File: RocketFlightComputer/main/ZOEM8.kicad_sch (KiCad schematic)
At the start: 11 parts

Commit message: Well I added a bunch of sensors, some connectors for battery, pyro channels mosfets, etc
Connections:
- net ZOEM8_SCL renamed ZOEM8_SCL1
- net ZOEM8_SDA renamed ZOEM8_SDA1
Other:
- note added: "Max Current: 67 mA"
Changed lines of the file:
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@@
     (effects (font (size 2.032 2.032)) (justify left bottom))
+  )
+  (text "Max Current: 67 mA" (at 177.8 161.29 0)
+    (effects (font (size 1.778 1.5113)) (justify left bottom))
   )
   (text "u.FL Connector" (at 112.395 127.635 0)
@@
     (effects (font (size 0.889 0.889)) (justify left bottom))
   )
-  (hierarchical_label "ZOEM8_SCL" (shape bidirectional) (at 208.915 59.69 0) (fields_autoplaced)
+  (hierarchical_label "ZOEM8_SCL1" (shape bidirectional) (at 208.915 59.69 0) (fields_autoplaced)
     (effects (font (size 1.27 1.27)) (justify left))
   )
-  (hierarchical_label "ZOEM8_SDA" (shape bidirectional) (at 190.5 57.15 0) (fields_autoplaced)
+  (hierarchical_label "ZOEM8_SDA1" (shape bidirectional) (at 190.5 57.15 0) (fields_autoplaced)
     (effects (font (size 1.27 1.27)) (justify left))
   )

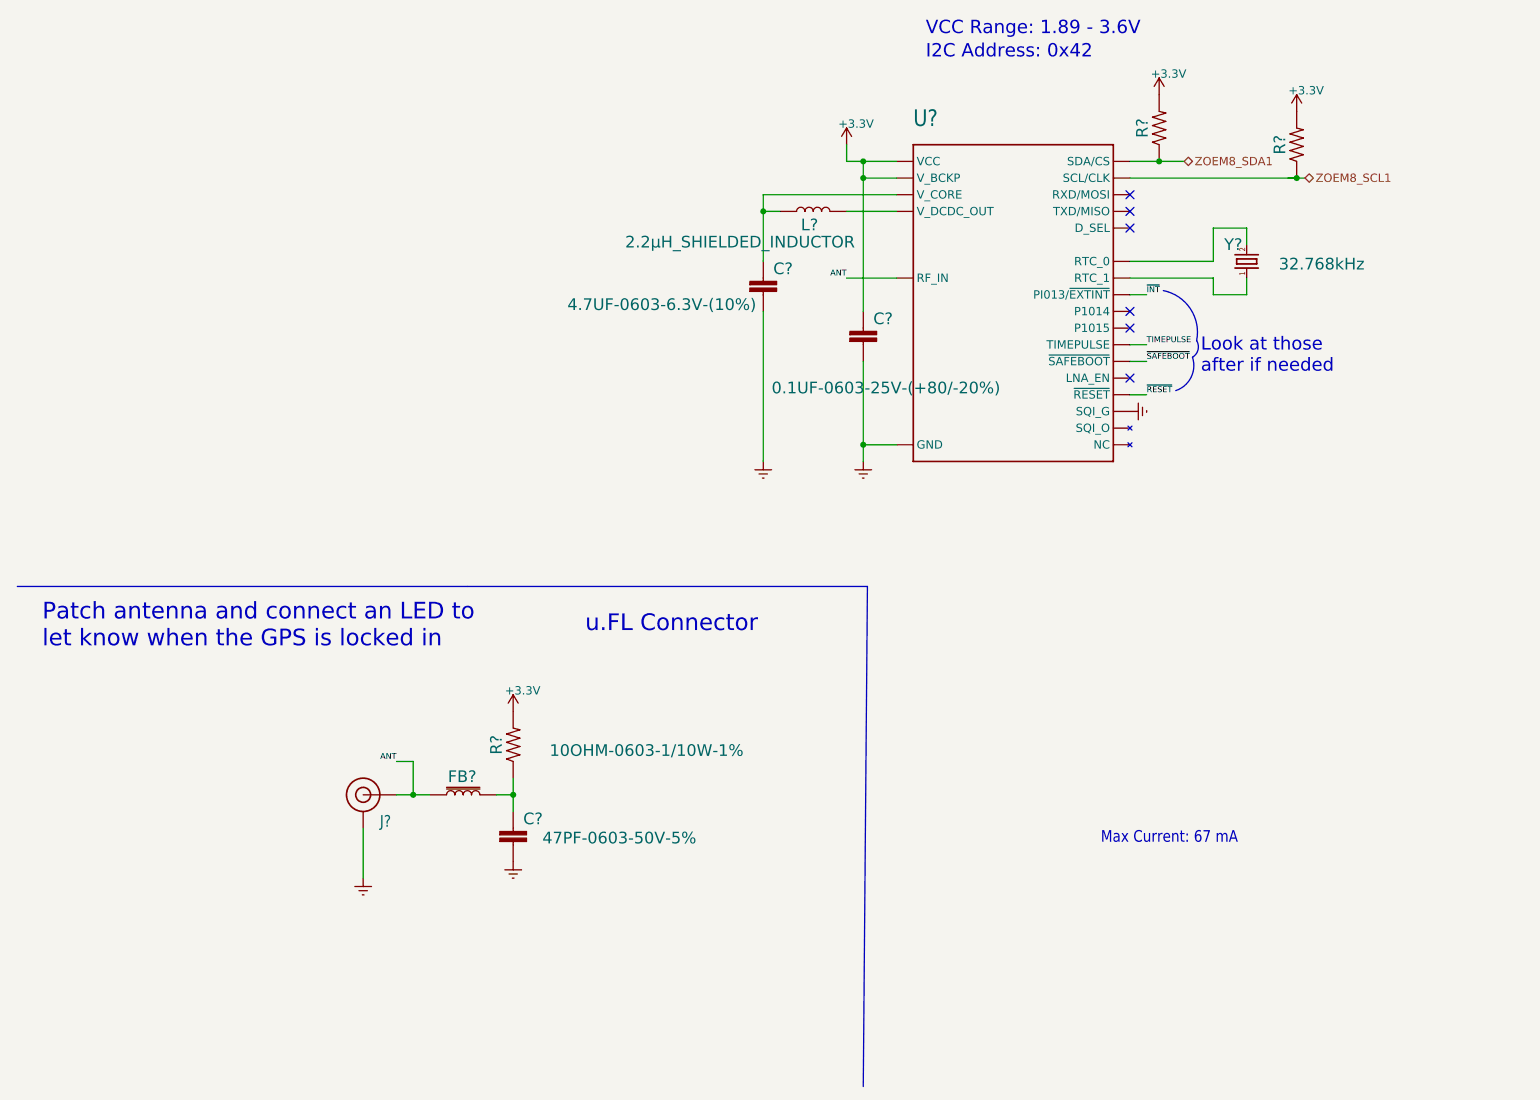
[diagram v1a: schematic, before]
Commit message: Addition of telemetry is pcb schematic
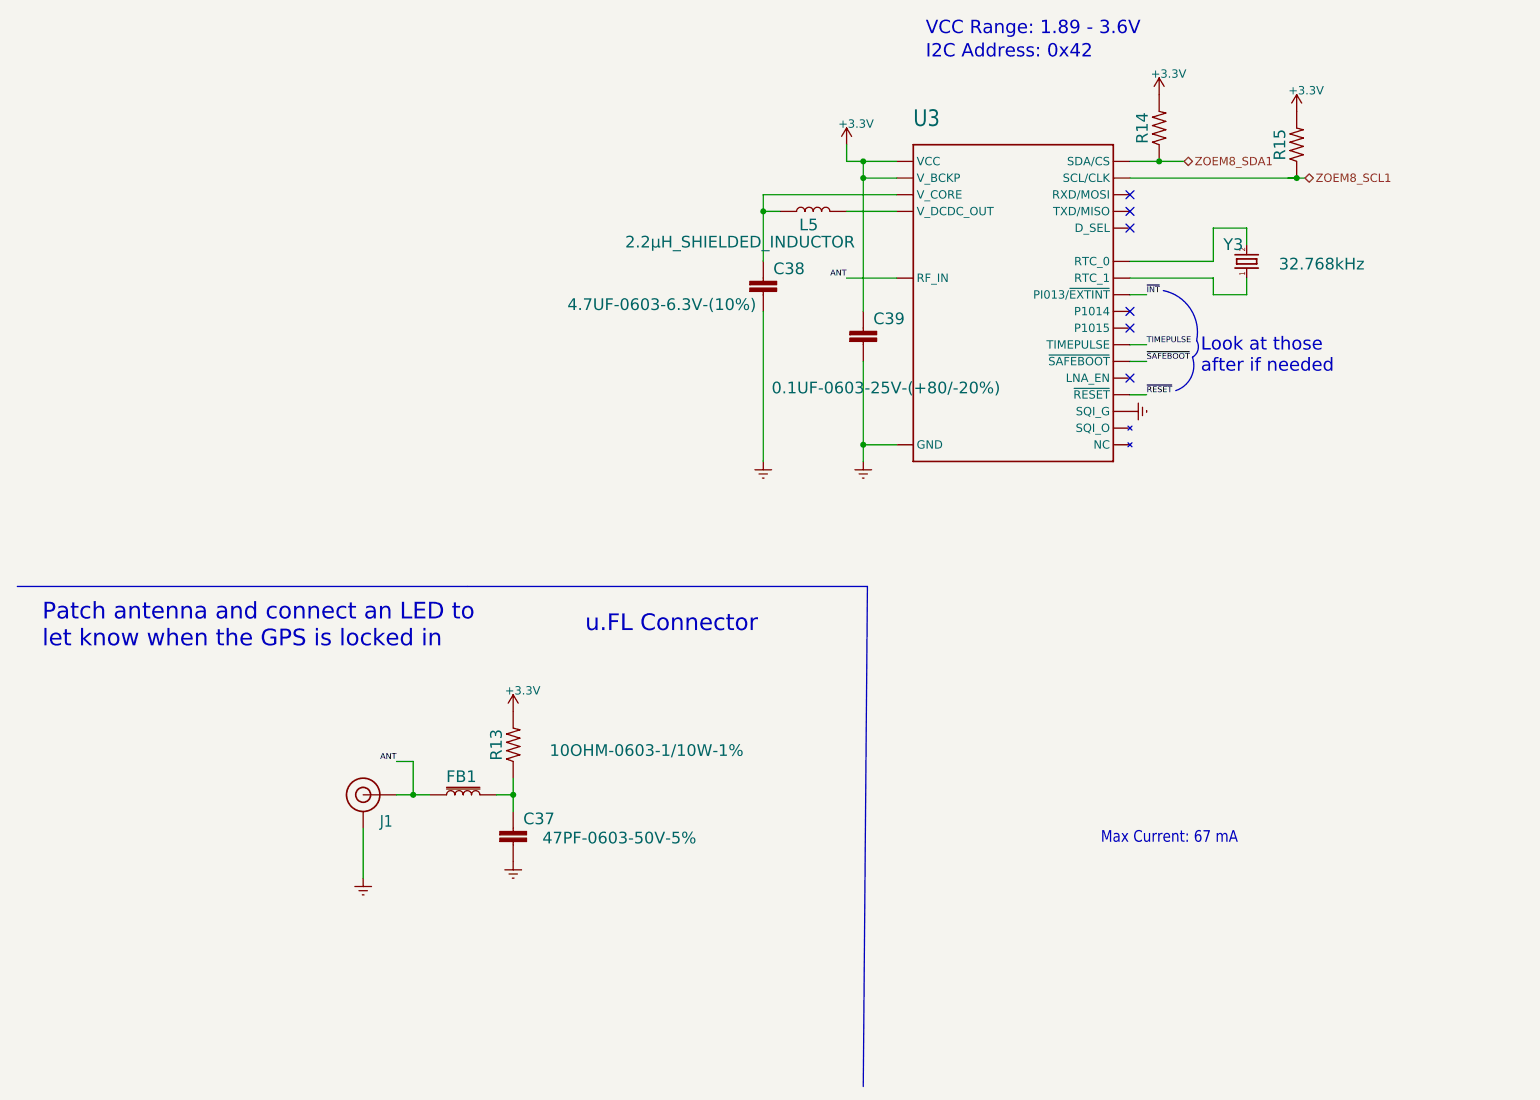
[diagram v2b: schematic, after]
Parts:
- gave numbers to parts that had none: 11

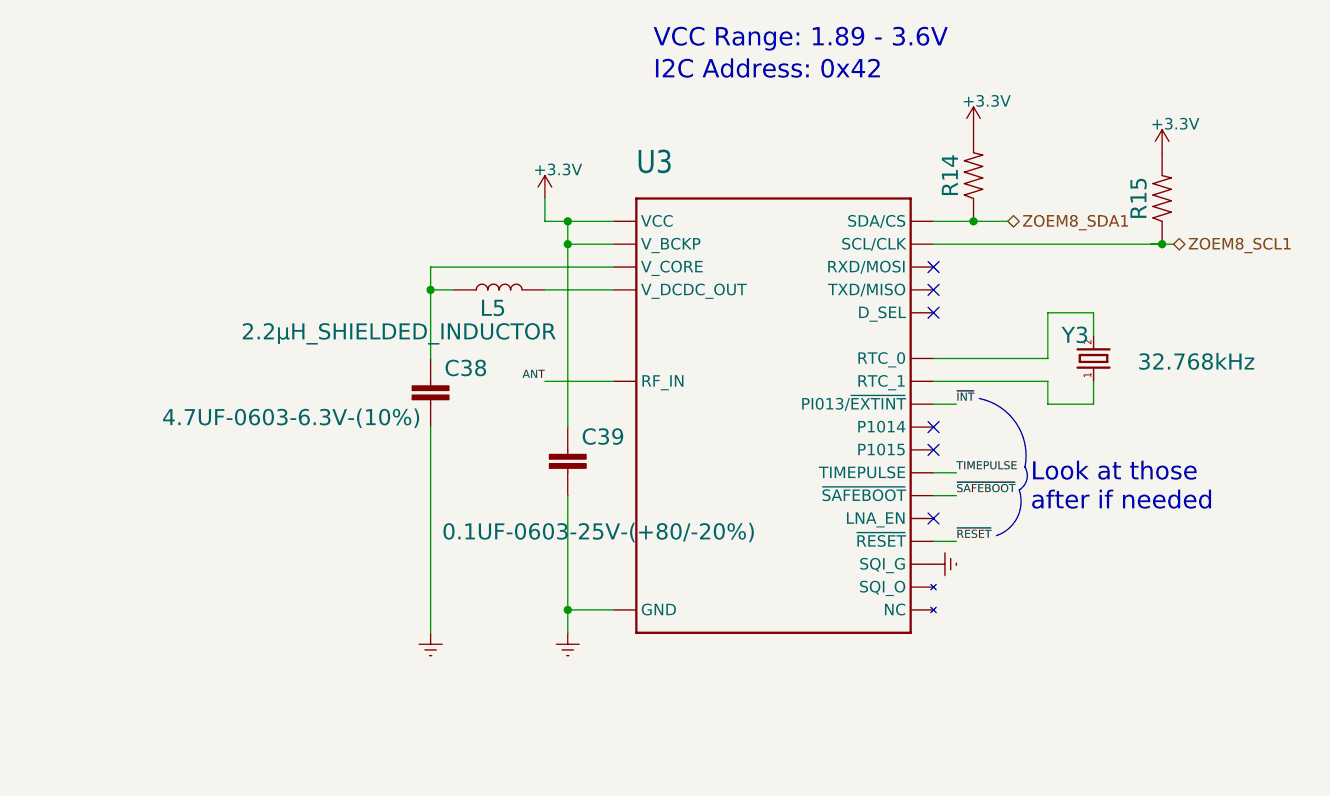
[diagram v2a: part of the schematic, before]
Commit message: The design is getting more mature, still did not choose if doing 4 layers or 2 layers pcb, will try to add 5v for a on board camera and trace routes for reserved pins in case of usage on another vehicle
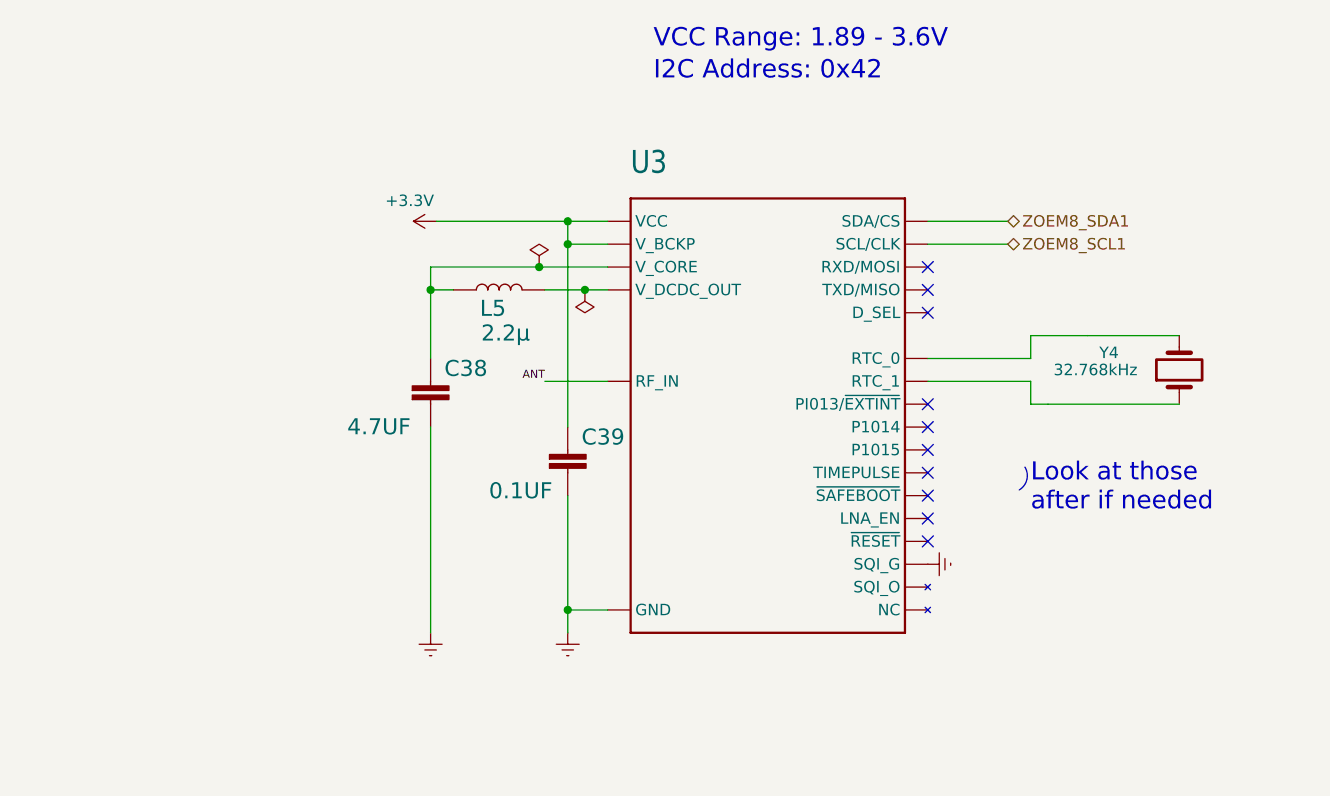
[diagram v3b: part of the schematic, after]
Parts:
- removed R14, R15: 2.2KOHM-0603-1/10W-1%, SparkFun_ZOE-M8Q GPS:0603, symbol SparkFun_ZOE-M8Q GPS-eagle-import:2.2KOHM-0603-1/10W-1%
- removed Y3: 32.768kHz, SparkFun_ZOE-M8Q GPS:CRYSTAL-SMD-3.2X1.5MM, symbol SparkFun_ZOE-M8Q GPS-eagle-import:CRYSTAL-32.768KHZSMD-3.2X1.5
- added Y4: 32.768kHz, Crystal:Crystal_SMD_2012-2Pin_2.0x1.2mm, symbol Device:Crystal
- C37, R13: footprint SparkFun_ZOE-M8Q GPS:0603 -> Resistor_SMD:R_0603_1608Metric_Pad0.98x0.95mm_HandSolder
- C38: value 4.7UF-0603-6.3V-(10%) -> 4.7UF; footprint SparkFun_ZOE-M8Q GPS:0603 -> Resistor_SMD:R_0603_1608Metric_Pad0.98x0.95mm_HandSolder
- C39: value 0.1UF-0603-25V-(+80/-20%) -> 0.1UF; footprint SparkFun_ZOE-M8Q GPS:0603 -> Resistor_SMD:R_0603_1608Metric_Pad0.98x0.95mm_HandSolder
- L5: value 2.2μH_SHIELDED_INDUCTOR -> 2.2μ; footprint SparkFun_ZOE-M8Q GPS:0806 -> Resistor_SMD:R_0603_1608Metric_Pad0.98x0.95mm_HandSolder
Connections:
- net at U3.19 (RTC_1): now also Y4.1
- net at U3.18 (RTC_0): now also Y4.2
- net TIMEPULSE: no longer names the net of U3.33 (TIMEPULSE)
- net ~{INT}: no longer names the net of U3.43 (PI013/~{EXTINT})
- net ~{RESET}: no longer names the net of U3.20 (~{RESET})
- net ~{SAFEBOOT}: no longer names the net of U3.34 (~{SAFEBOOT})
- no-connect marks 6 -> 10
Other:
- moved on the sheet: U3

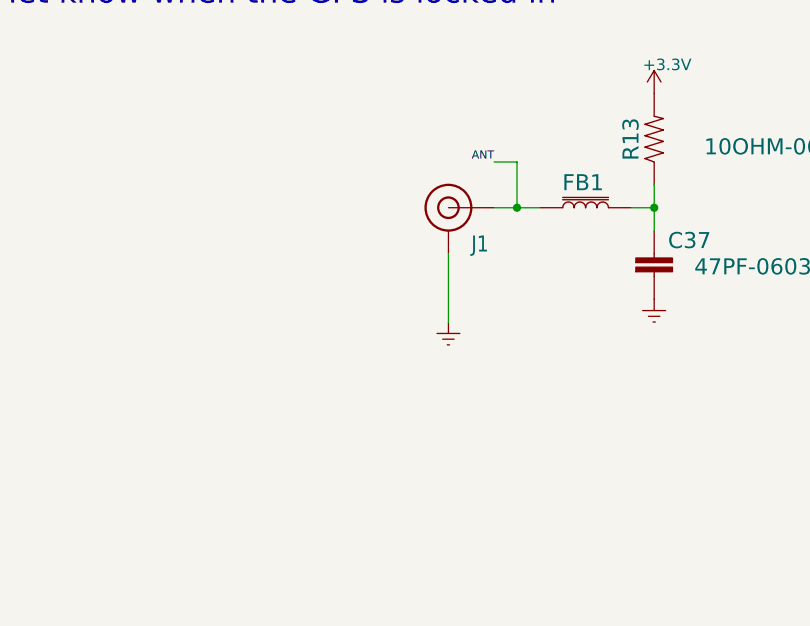
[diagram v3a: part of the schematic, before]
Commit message: CID documentation and started the PCB editor process
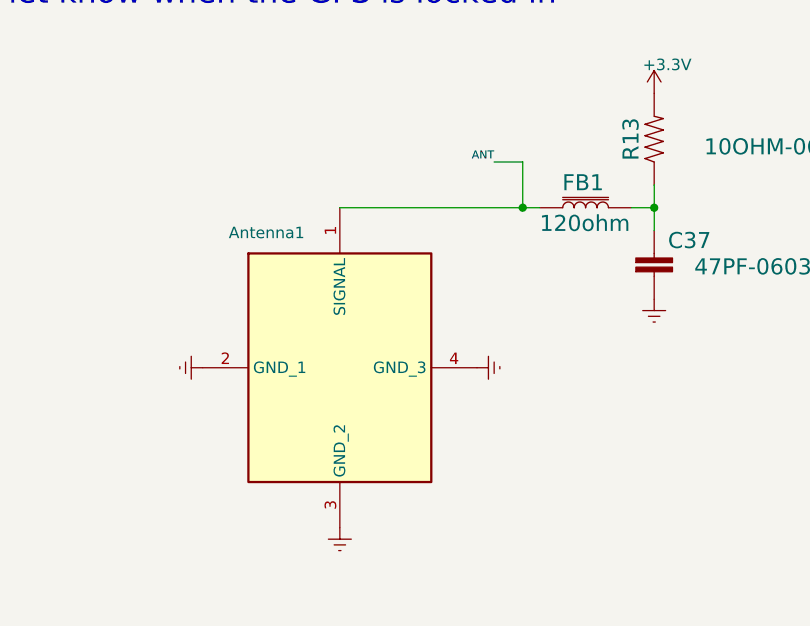
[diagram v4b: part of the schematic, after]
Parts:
- removed J1: U.FL, ZOE-M8Q:U.FL, symbol SparkFun_ZOE-M8Q GPS-eagle-import:U.FL2PIN
- added Antenna1: CONMHF1-SMD-G-T, footprint:CONMHF1SMDGT, symbol CONMHF1-SMD-G-T:CONMHF1-SMD-G-T
- FB1: value FERRITE_BEAD-120_OHM-0402 -> 120ohm; footprint ZOE-M8Q:0402 -> Resistor_SMD:R_0603_1608Metric_Pad0.98x0.95mm_HandSolder
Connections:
- net ANT: now also Antenna1.1 (SIGNAL)
- net GNDREF: now also Antenna1.2 (GND_1), Antenna1.3 (GND_2), Antenna1.4 (GND_3)
